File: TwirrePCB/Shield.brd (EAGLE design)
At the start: 87.3 x 53.3 mm, 38 parts, among them Q1 BSS138, Q2 BSS138, T2 BC847, U1 ARDUINO-MEGAPRO

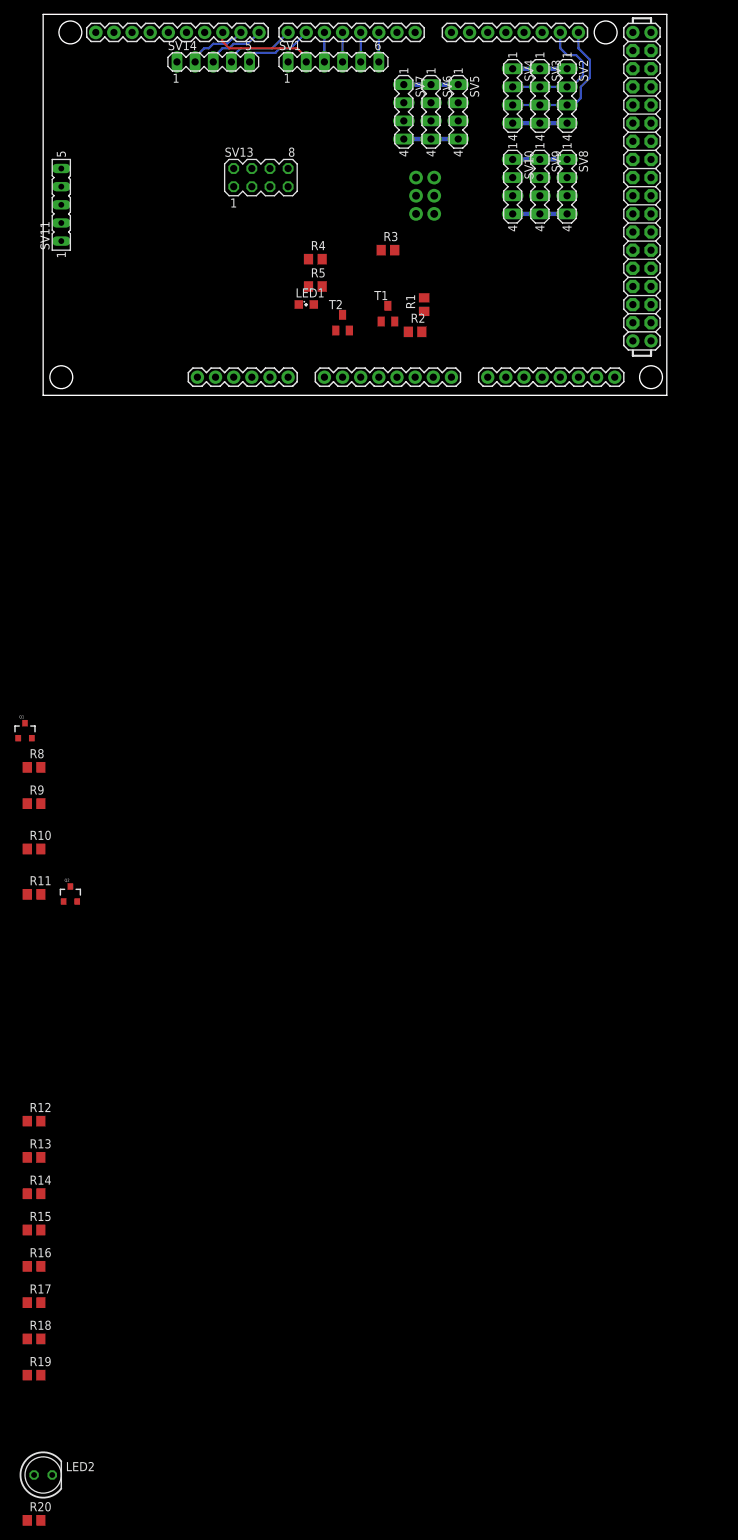
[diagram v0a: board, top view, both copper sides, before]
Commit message: Add various components to library
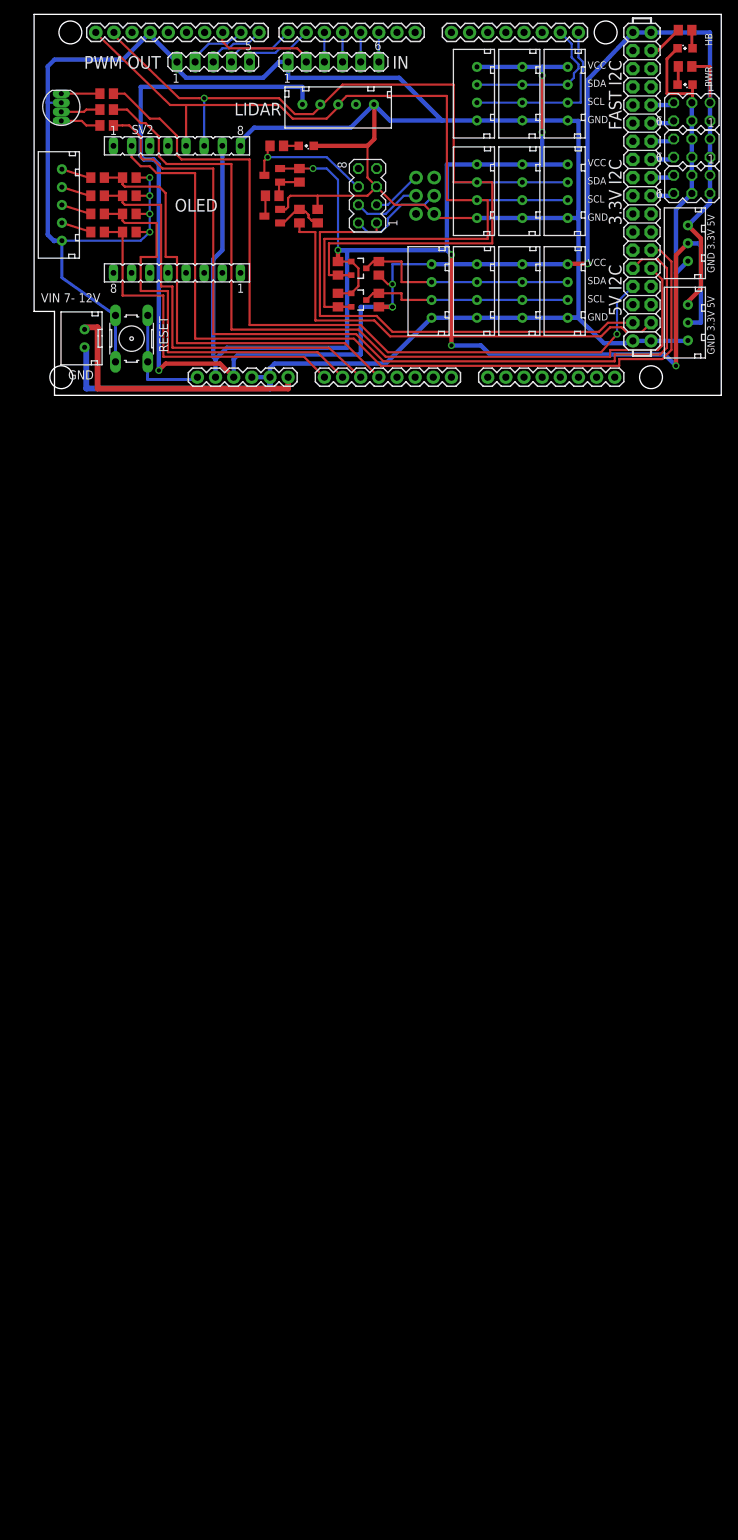
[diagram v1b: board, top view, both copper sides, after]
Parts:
- removed SV10, SV7, SV8, SV9: (no value), con-lstb:MA04-1
- removed SV11: LIPO, con-lsta:FE05-1
- added LED3: (no value), led:SML0805
- added R21, R6, R7: 100, resistor:R0805
- added R22: (no value), resistor:R0805
- added S1: (no value), switch-omron:B3F-10XX
- added U$1: RGB5MMRGB5MM, Arduino-Boards:RGB5MM
- added U$10, U$11, U$2, U$3, U$4, U$5, U$6, U$7, U$8, U$9: JST-4, Arduino-Boards:JST-4
- added U$12, U$13: LIDAR, Arduino-Boards:JST-5
- added U$14, U$15: JST-3, Arduino-Boards:JST-3
- added U$16: JST-2, Arduino-Boards:JST-2
- LED2: device led:LED5MM -> led:SML0805
- SV2, SV3: device con-lstb:MA04-1 -> con-lsta:FE08
- SV4, SV5, SV6: device con-lstb:MA04-1 -> con-lstb:MA03-2
- moved LED2 219.0 mm to (89.9, 48.6)
- moved R20 200.0 mm to (8.89, 42.2)
- moved R19 168.2 mm to (12.1, 30.5), turned to 180 degrees
- moved R18 162.8 mm to (7.62, 30.5), turned to 180 degrees
- moved R17 155.5 mm to (12.1, 27.9), turned to 180 degrees
- moved R16 150.1 mm to (7.62, 27.9), turned to 180 degrees
- moved R15 142.9 mm to (12.1, 25.4), turned to 180 degrees
- moved R14 137.4 mm to (7.62, 25.4), turned to 180 degrees
- moved R13 130.2 mm to (12.1, 22.9), turned to 180 degrees
- moved R12 124.8 mm to (7.62, 22.9), turned to 180 degrees
- moved R11 96.2 mm to (47.0, 13.3), turned to 270 degrees
- moved Q2 92.4 mm to (44.1, 13.3), turned to 270 degrees
- moved R9 89.1 mm to (47.0, 17.8), turned to 270 degrees
- moved R10 87.8 mm to (41.3, 13.3), turned to 90 degrees
- moved R8 81.8 mm to (41.3, 17.8), turned to 90 degrees
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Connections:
- new net N$20: R7.2, U1.46
- new net N$21: R20.1, U$1.P3
- new net N$22: R6.1, U$1.P2
- new net N$23: R7.1, U$1.P1
- new net N$24: SV2.2, U1.45
- new net N$25: SV5.6, U1.35
- new net N$26: SV5.5, U1.33
- new net N$27: SV4.6, U1.31
- new net N$28: SV6.6, U1.39
- new net N$29: SV6.5, U1.37
- new net N$30: LED2.A, R21.2
- new net N$31: SV4.5, U1.29
- new net N$32: R21.1, U1.23
- new net N$33: LED3.A, R22.2
- new net N$34: S1.1, S1.2, U1.RESET
- new net N$35: U$16.2, U1.VIN
- net +3V3: now also SV2.7, U$10.4, U$14.2, U$15.2, U$2.4, U$3.4, U$4.4, U$8.4, U$9.4, U1.3.3V; no longer SV10.1, SV2.1, SV3.1, SV4.1, SV8.1, SV9.1
- net +5V: now also R22.1, SV4.1, SV4.2, SV5.2, SV6.2, U$11.4, U$12.5, U$14.3, U$15.3, U$5.4, U$6.4, U$7.4, U1.5V@0, U1.5V@1, U1.5V@2; no longer SV7.1
- net GND: now also LED2.C, LED3.C, S1.3, S1.4, SV2.8, SV4.3, SV5.3, SV6.3, U$1.C, U$10.1, U$11.1, U$12.1, U$13.1, U$14.1, U$15.1, U$16.1, U$2.1, U$3.1, U$4.1, U$5.1, U$6.1, U$7.1, U$8.1, U$9.1; no longer LED2.K, SV10.4, SV11.1, SV2.4, SV3.4, SV7.4, SV8.4, SV9.4
- net N$10: now also U$13.3; no longer SV11.3
- net N$11: now also U$13.4; no longer SV11.4
- net N$12: now also U$13.5; no longer SV11.5
- net N$15: now also R6.2, U1.47; no longer LED2.A, R20.1
- net N$7: now also U$13.2; no longer SV11.2
- net SCL_HS: now also U$10.2, U$8.2, U$9.2, U1.21; no longer SV10.3, SV8.3, SV9.3, U1.SCL_HS
- net SCL_LS: now also SV2.5, U$12.3, U$2.2, U$3.2, U$4.2, U1.SCL_HS; no longer SV2.3, SV3.3, SV4.3, U1.21
- net SCL_LS_5: now also U$11.2, U$5.2, U$6.2, U$7.2; no longer SV5.3, SV6.3, SV7.3
- net SDA_HS: now also U$10.3, U$8.3, U$9.3, U1.20; no longer SV10.2, SV8.2, SV9.2, U1.SDA_HS
- net SDA_LS: now also SV2.6, U$12.4, U$2.3, U$3.3, U$4.3, U1.SDA_HS; no longer SV2.2, SV3.2, SV4.2, U1.20
- net SDA_LS_5: now also U$11.3, U$5.3, U$6.3, U$7.3; no longer SV5.2, SV6.2, SV7.2
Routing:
- net GND: track 22.9 -> 441.9 mm, vias 0 -> 4
- net +5V: track 7.62 -> 243.8 mm, vias 0 -> 5
- net +3V3: track 15.2 -> 245.4 mm, vias 0 -> 7
- net N$20: track 0.00 -> 124.7 mm
- net N$24: track 0.00 -> 120.2 mm
- net N$15: track 0.00 -> 119.0 mm
- net SDA_LS: track 18.6 -> 137.0 mm, vias 0 -> 1
- net SCL_LS: track 20.3 -> 137.8 mm
- net N$14: track 0.00 -> 109.4 mm, vias 0 -> 1
- net SPI_CS: track 0.00 -> 66.2 mm
- net FLIR_PWR: track 0.00 -> 65.1 mm
- net LIPO_C4: track 0.00 -> 62.9 mm
- net LIPO_C3: track 0.00 -> 58.6 mm
- net LIPO_C2: track 0.00 -> 58.4 mm
- net LIPO_C1: track 0.00 -> 50.3 mm
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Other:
- board size 87.3 x 53.3 mm -> 96.2 x 53.3 mm
- board text added: "3.3V I2C"
- board text added: "5V I2C"
- board text added: "FAST I2C"
- board text added: "GND"
- board text added: "GND 3.3V 5V"
- board text added: "HB"
- board text added: "IN"
- board text added: "LIDAR"
- board text added: "OLED"
- board text added: "PWM OUT"
- board text added: "PWR"
- board text added: "RESET"
- board text added: "SCL"
- board text added: "SDA"
- board text added: "VCC"
- board text added: "VIN 7- 12V"

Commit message: Add caps and lots of other stuff
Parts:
- removed SV1: PWM IN, con-lstb:MA06-1
- removed SV14: PWM OUT, con-lstb:MA05-1
- removed SV4, SV5, SV6: (no value), con-lstb:MA03-2
- added C1: 560uF, resistor:153CLV-1010
- added C2: (no value), resistor:153CLV-0605
- added U$17: JST-6, Arduino-Boards:JST-6
- added U$18: JST-5, Arduino-Boards:JST-5
- added U$19, U$20, U$21, U$22, U$23, U$24: SERVOHEADER, Arduino-Boards:SERVOHEADER
- R22: value (none) -> 220
- moved U$12 4.24 mm to (38.4, 39.4)
- moved R13 1.91 mm to (14.0, 22.9)
- moved R15 1.91 mm to (14.0, 25.4)
- moved R17 1.91 mm to (14.0, 27.9)
- moved R19 1.91 mm to (14.0, 30.5)
- moved R12 1.27 mm to (8.89, 22.9)
- moved R14 1.27 mm to (8.89, 25.4)
- moved R16 1.27 mm to (8.89, 27.9)
- moved R18 1.27 mm to (8.89, 30.5)
- moved U$13 0.63 mm to (2.86, 25.4)
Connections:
- removed net N$31: SV4.5, U1.29
- new net N$36: U$24.S, U1.29
- net +3V3: now also C2.+
- net +5V: now also C1.+, U$19.+, U$20.+, U$21.+, U$22.+, U$23.+, U$24.+; no longer SV4.1, SV4.2, SV5.1, SV5.2, SV6.1, SV6.2
- net GND: now also C1.-, C2.-, U$17.1, U$18.1, U$19.-, U$20.-, U$21.-, U$22.-, U$23.-, U$24.-; no longer SV1.1, SV14.1, SV4.3, SV4.4, SV5.3, SV5.4, SV6.3, SV6.4
- net N$13: now also U$17.6; no longer SV1.2
- net N$16: now also U$18.2; no longer SV14.5
- net N$17: now also U$18.3; no longer SV14.4
- net N$18: now also U$18.4; no longer SV14.3
- net N$19: now also U$18.5; no longer SV14.2
- net N$25: now also U$21.S; no longer SV5.6
- net N$26: now also U$22.S; no longer SV5.5
- net N$27: now also U$23.S; no longer SV4.6
- net N$28: now also U$19.S; no longer SV6.6
- net N$29: now also U$20.S; no longer SV6.5
- net N$5: now also U$17.5, U1.5; no longer SV1.6, U1.2
- net N$6: now also U$17.4, U1.4; no longer SV1.5, U1.3
- net N$8: now also U$17.3, U1.3; no longer SV1.4, U1.4
- net N$9: now also U$17.2, U1.2; no longer SV1.3, U1.5
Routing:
- net +5V: track 243.8 -> 255.5 mm, vias 5 -> 6
- net SDA_LS: track 137.0 -> 126.7 mm
- net N$16: track 10.2 -> 18.2 mm
- net GND: track 441.9 -> 433.9 mm, vias 4 -> 5
- net N$13: track 14.6 -> 7.30 mm
- net N$17: track 10.0 -> 17.0 mm
- net N$18: track 8.50 -> 15.5 mm
- net N$19: track 8.50 -> 15.4 mm
- net SCL_LS: track 137.8 -> 130.9 mm
- net N$9: track 4.13 -> 9.13 mm
- net N$8: track 4.13 -> 9.09 mm
- net N$6: track 4.13 -> 9.05 mm
- net N$5: track 4.13 -> 9.01 mm
- net N$15: track 119.0 -> 114.6 mm
- net SPI_MOSI: track 13.8 -> 18.2 mm
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- added copper zone on layer 1, net GND
- added copper zone on layer 16, net GND
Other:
- board size 96.2 x 53.3 mm -> 96.2 x 53.6 mm
- board text added: "BALANCE"
- board text added: "STATUS"

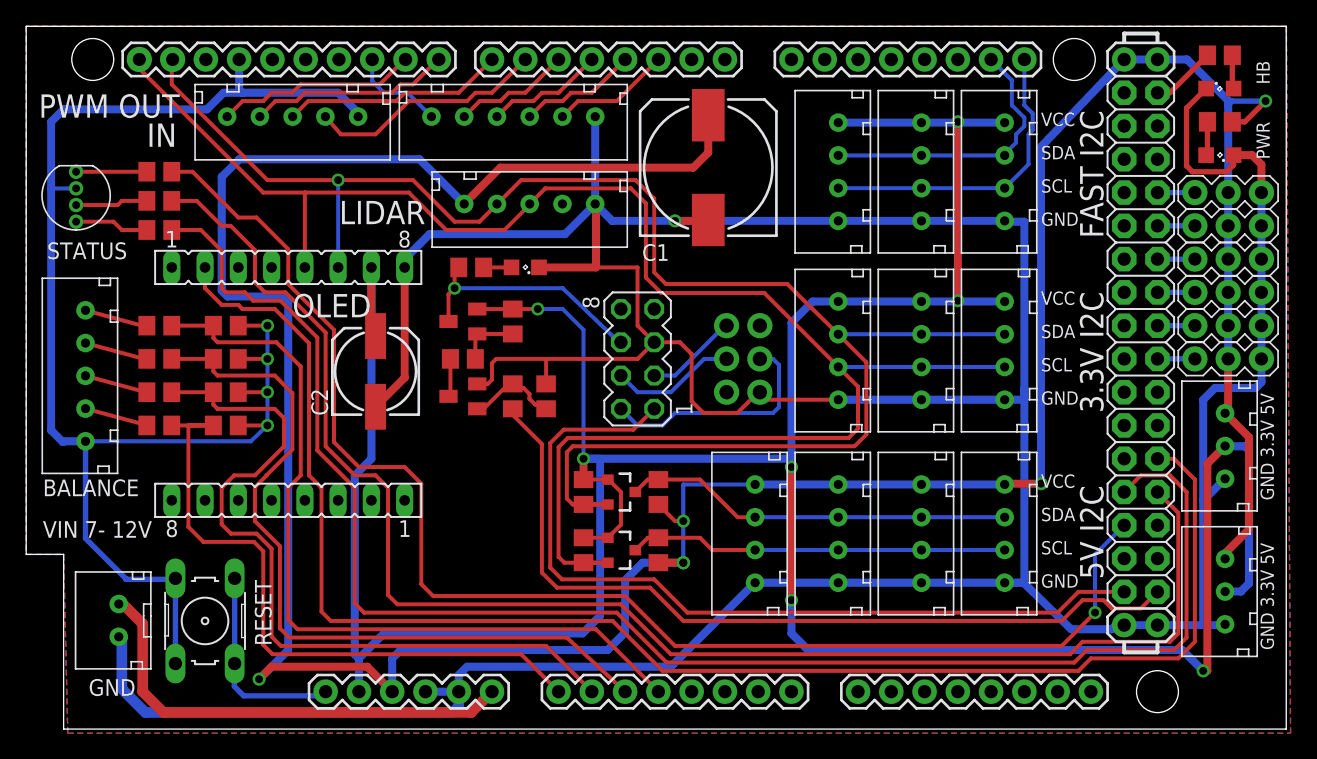
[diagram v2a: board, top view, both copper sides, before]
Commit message: Move some parts and wires around, finished first revision
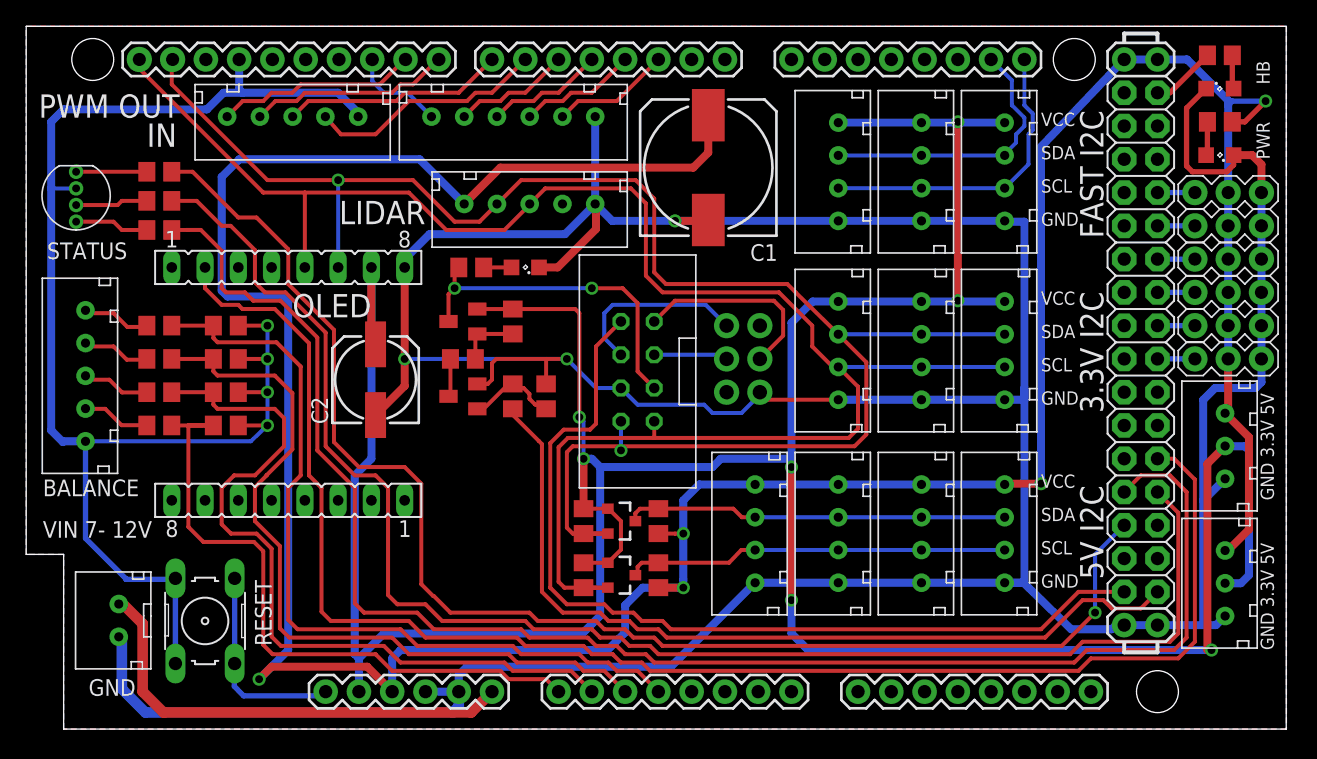
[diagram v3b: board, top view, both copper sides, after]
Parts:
- removed SV13: (no value), con-lstb:MA04-2
- added U$25: IDC-8WAY, Arduino-Boards:IDC-8WAY
- C2: value (none) -> 47uF
- moved Q1 2.22 mm to (44.1, 15.6)
- moved R8 2.22 mm to (41.3, 15.6)
- moved R9 2.22 mm to (47.0, 15.6)
- moved Q2 1.91 mm to (44.1, 11.4)
- moved R10 1.91 mm to (41.3, 11.4)
- moved R11 1.91 mm to (47.0, 11.4)
- moved C2 0.64 mm to (25.4, 26.4)
- moved U$15 0.63 mm to (89.9, 12.1)
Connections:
- removed net SCL: SV13.8
- removed net SDA: SV13.7
- net GND: now also U$25.5; no longer SV13.5
- net SCL_LS: now also U$25.8
- net SDA_LS: now also U$25.7
- net SPI_CLK: now also U$25.4; no longer SV13.4
- net SPI_CS: now also U$25.1; no longer SV13.1
- net SPI_MISO: now also U$25.3; no longer SV13.3
- net SPI_MOSI: now also U$25.2; no longer SV13.2
- net SPI_VIN: now also U$25.6; no longer SV13.6
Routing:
- net SPI_VIN: track 19.0 -> 26.1 mm, vias 1 -> 2
- net SPI_MISO: track 7.10 -> 14.0 mm
- net SPI_CS: track 64.4 -> 70.0 mm
- net SDA_LS: track 126.7 -> 131.4 mm, vias 1 -> 2
- net SCL_LS: track 130.9 -> 135.1 mm
- net SPI_CLK: track 9.64 -> 5.84 mm
- net +5V: track 255.5 -> 252.2 mm, vias 6 -> 5
- net SPI_MOSI: track 18.2 -> 15.3 mm
- net FLIR_PWR: track 63.4 -> 65.3 mm
- net SDA_LS_5: track 30.4 -> 29.2 mm
- net GND: track 433.9 -> 433.0 mm, vias 5 -> 7
- net N$10: track 4.87 -> 5.50 mm
- net N$11: track 4.91 -> 5.51 mm
- net +3V3: track 248.5 -> 247.9 mm
- net N$12: track 4.95 -> 5.53 mm
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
